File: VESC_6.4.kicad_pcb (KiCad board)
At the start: 4 copper layers, 62 x 60 mm, 389 parts, among them J1 CAN, J10 SUPPLY, J11 GND, J2 HALL_ENC, J3 COMM, J4 SERVO, J5 SWD, J6 USB_OTG, J7 PH_A, J8 PH_B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

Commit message: sometimes the gremlins would delete all of the save buttons work!
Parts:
- moved SW1 0.44 mm to (128.7, 67.2)
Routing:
- net /MCU/HALL_3: track 20.6 -> 58.7 mm, vias 0 -> 2
- net /MCU/HALL_2: track 16.5 -> 52.4 mm, vias 0 -> 2
- net /DRV/SDO: track 0.00 -> 30.3 mm, vias 0 -> 2
- net /DRV/SDI: track 0.00 -> 29.1 mm, vias 0 -> 2
- net /DRV/SCLK: track 0.00 -> 28.1 mm, vias 0 -> 2
- net /DRV/FAULT: track 0.00 -> 28.0 mm, vias 0 -> 2
- net /DRV/EN_GATE: track 0.00 -> 24.6 mm, vias 0 -> 3
- net /MCU/HALL_1: track 12.8 -> 33.6 mm, vias 0 -> 1
- net /MCU/ADC_TEMP: track 8.85 -> 25.4 mm, vias 0 -> 4
- net /DRV/CS: track 0.00 -> 3.13 mm, vias 0 -> 1
- net /MCU/H2: track 0.00 -> 3.07 mm, vias 0 -> 1
- net /MCU/H1: track 0.00 -> 2.75 mm, vias 0 -> 1
- net /MCU/H3: track 0.00 -> 2.60 mm, vias 0 -> 1
- net /MCU/TEMP_MOTOR: track 65.6 -> 66.4 mm
- net /DRV/INL_C: track 24.8 -> 24.3 mm

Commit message: dun dun dun
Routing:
- net /MCU/HALL_1: track 33.6 -> 69.4 mm, vias 1 -> 2
- net /DRV/CS: track 3.13 -> 32.2 mm, vias 1 -> 2
- net /MCU/H1: track 2.75 -> 27.2 mm, vias 1 -> 2
- net /MCU/HALL_2: track 52.4 -> 74.7 mm
- net /MCU/HALL_3: track 58.7 -> 80.2 mm
- net /DRV/EN_GATE: track 24.6 -> 25.8 mm
- net /DRV/FAULT: track 28.0 -> 28.7 mm
- net /DRV/SCLK: track 28.1 -> 28.8 mm
- net /DRV/SDI: track 29.1 -> 29.7 mm
- net /DRV/SDO: track 30.3 -> 30.9 mm

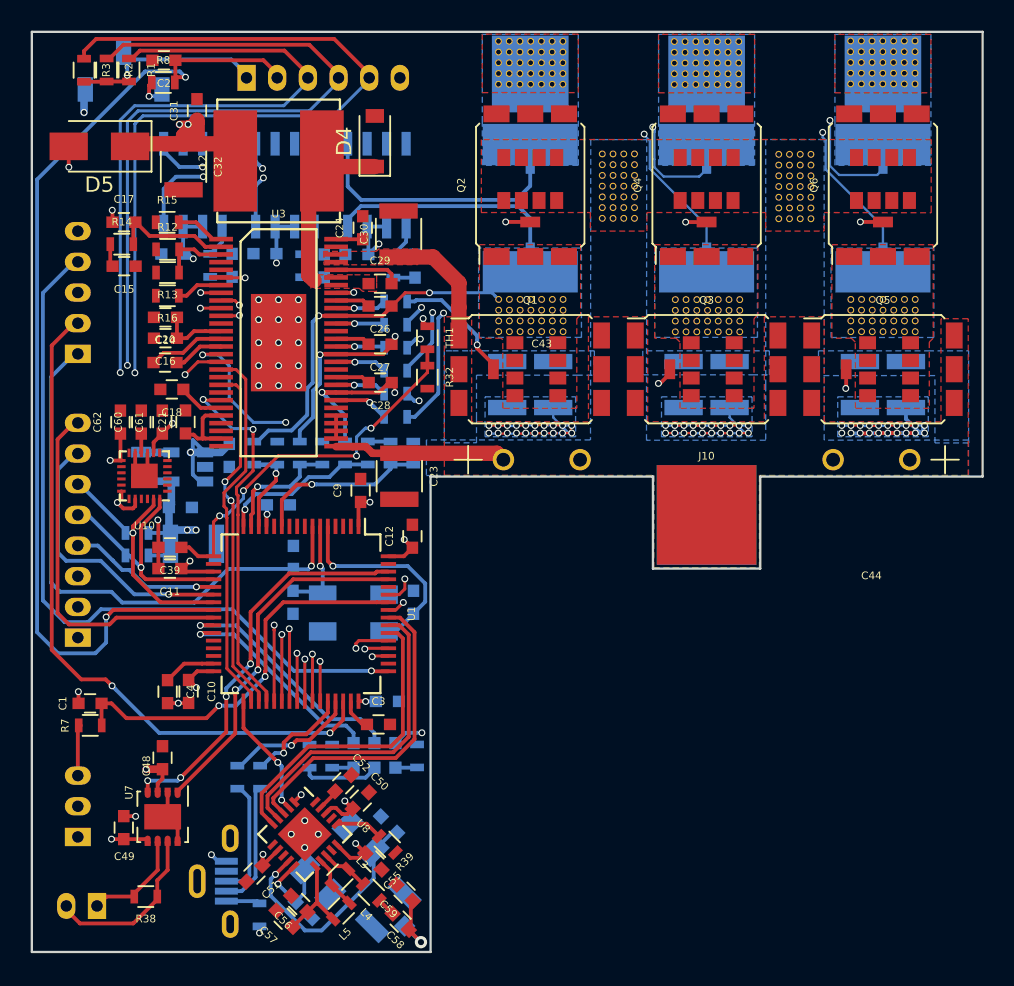
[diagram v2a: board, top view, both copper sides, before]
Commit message: something ate the power electronics ground plane!
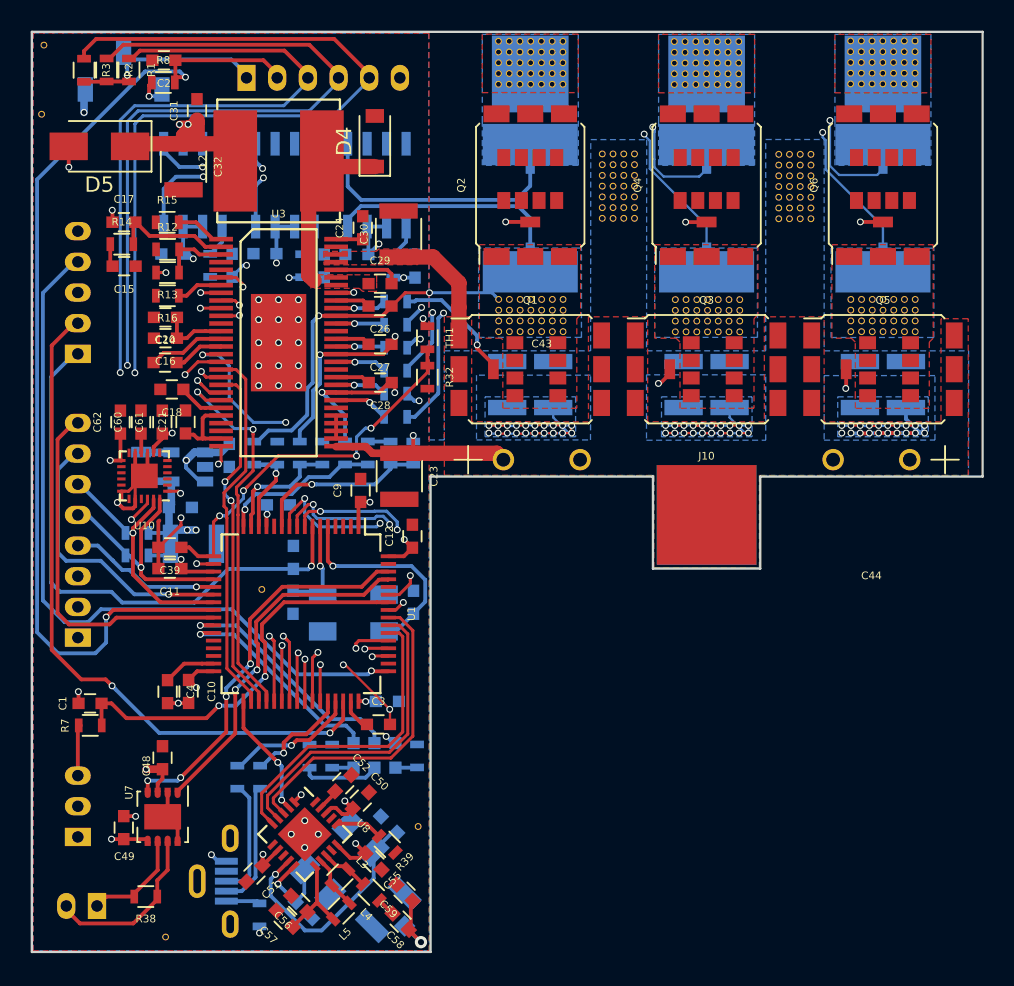
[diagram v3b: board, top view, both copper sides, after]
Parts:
- added ?: , Global_Parts:via-0.45mm, F.Cu at (137.7, 101.0)
- added ?: , Global_Parts:via-0.45mm, F.Cu at (131.4, 123.6)
- added ?: , Global_Parts:via-0.45mm, F.Cu at (147.9, 116.4)
- added ?: , Global_Parts:via-0.45mm, F.Cu at (123.3, 70.0)
- added ?: , Global_Parts:via-0.45mm, F.Cu at (123.5, 65.5)
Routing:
- net /MCU/CURRENT_3: track 1.43 -> 33.8 mm, vias 0 -> 3
- net /MCU/CURRENT_2: track 1.45 -> 30.9 mm, vias 0 -> 3
- net /MCU/CURRENT_1: track 1.42 -> 30.3 mm, vias 0 -> 3
- net /MCU/H3: track 2.60 -> 26.4 mm, vias 1 -> 2
- net /MCU/H2: track 3.07 -> 26.7 mm, vias 1 -> 2
- net GND: track 36.8 -> 49.4 mm, vias 27 -> 31
- net +5V: track 125.7 -> 134.2 mm, vias 6 -> 7
- net SUPPLY: track 59.1 -> 61.4 mm, vias 60 -> 61
- net /DRV/INL_C: track 24.2 -> 25.4 mm
- net VCC: track 59.5 -> 60.5 mm, vias 22 -> 24
- net /MCU/HALL_3: track 80.2 -> 79.2 mm
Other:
- net class Default: clearance 0.13 -> 0
- rule trace_clearance: 0.13 -> 0

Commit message: Rev1a done
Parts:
- added ?: MountingHole_3.2mm_M3, Mounting_Holes:MountingHole_3.2mm_M3, F.Cu at (161.0, 67.1)
- added ?: , Global_Parts:via-0.45mm, F.Cu at (144.9, 93.6)
- added ?: , Global_Parts:via-0.45mm, F.Cu at (147.6, 93.9)
- added ?: , Global_Parts:via-0.45mm, F.Cu at (138.6, 75.3)
- added ?: , Global_Parts:via-0.45mm, F.Cu at (144.5, 74.6)
- added ?: , Global_Parts:via-0.45mm, F.Cu at (146.7, 74.5)
- added ?: , Global_Parts:via-0.45mm, F.Cu at (128.2, 112.4)
- added ?: , Global_Parts:via-0.45mm, F.Cu at (139.2, 123.9)
- added ?: , Global_Parts:via-0.45mm, F.Cu at (143.3, 123.9)
- added ?: , Global_Parts:via-0.45mm, F.Cu at (147.8, 119.4)
- added ?: , Global_Parts:via-0.45mm, F.Cu at (146.3, 113.7)
- added ?: MountingHole_3.2mm_M3, Mounting_Holes:MountingHole_3.2mm_M3, F.Cu at (172.5, 67.1)
- added ?: , Global_Parts:via-0.45mm, F.Cu at (148.0, 106.8)
- added ?: , Global_Parts:via-0.45mm, F.Cu at (137.2, 81.1)
- added ?: , Global_Parts:via-0.45mm, F.Cu at (138.3, 80.3)
- added ?: , Global_Parts:via-0.45mm, F.Cu at (139.9, 89.1)
- added ?: , Global_Parts:via-0.45mm, F.Cu at (130.6, 85.3)
- added ?: , Global_Parts:via-0.45mm, F.Cu at (130.0, 81.8)
- added ?: , Global_Parts:via-0.45mm, F.Cu at (131.3, 104.0)
- added ?: , Global_Parts:via-0.45mm, F.Cu at (129.1, 106.1)
- added ?: , Global_Parts:via-0.45mm, F.Cu at (129.3, 110.5)
- added ?: , Global_Parts:via-0.45mm, F.Cu at (136.5, 111.1)
- added ?: , Global_Parts:via-0.45mm, F.Cu at (134.4, 114.1)
- added ?: , Global_Parts:via-0.45mm, F.Cu at (137.3, 98.2)
- added ?: , Global_Parts:via-0.45mm, F.Cu at (144.4, 98.5)
- added ?: , Global_Parts:via-0.45mm, F.Cu at (146.4, 83.6)
- added ?: , Global_Parts:via-0.45mm, F.Cu at (146.4, 86.3)
- added ?: , Global_Parts:via-0.45mm, F.Cu at (129.4, 68.6)
- moved R38 1.01 mm to (130.2, 122.0), turned to 90 degrees
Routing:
- net GND: track 49.4 -> 64.0 mm, vias 31 -> 35
- net /DRV/SH_A: track 23.5 -> 31.8 mm
- net /DRV/SH_B: track 30.5 -> 34.5 mm
- net +5V: track 134.2 -> 130.5 mm
- net /DRV/SH_C: track 40.7 -> 42.5 mm
- net /CAN/CANL: track 6.77 -> 7.55 mm
- net /CAN/CANH: track 11.4 -> 12.0 mm
- added copper zone on F.Cu, net +5V

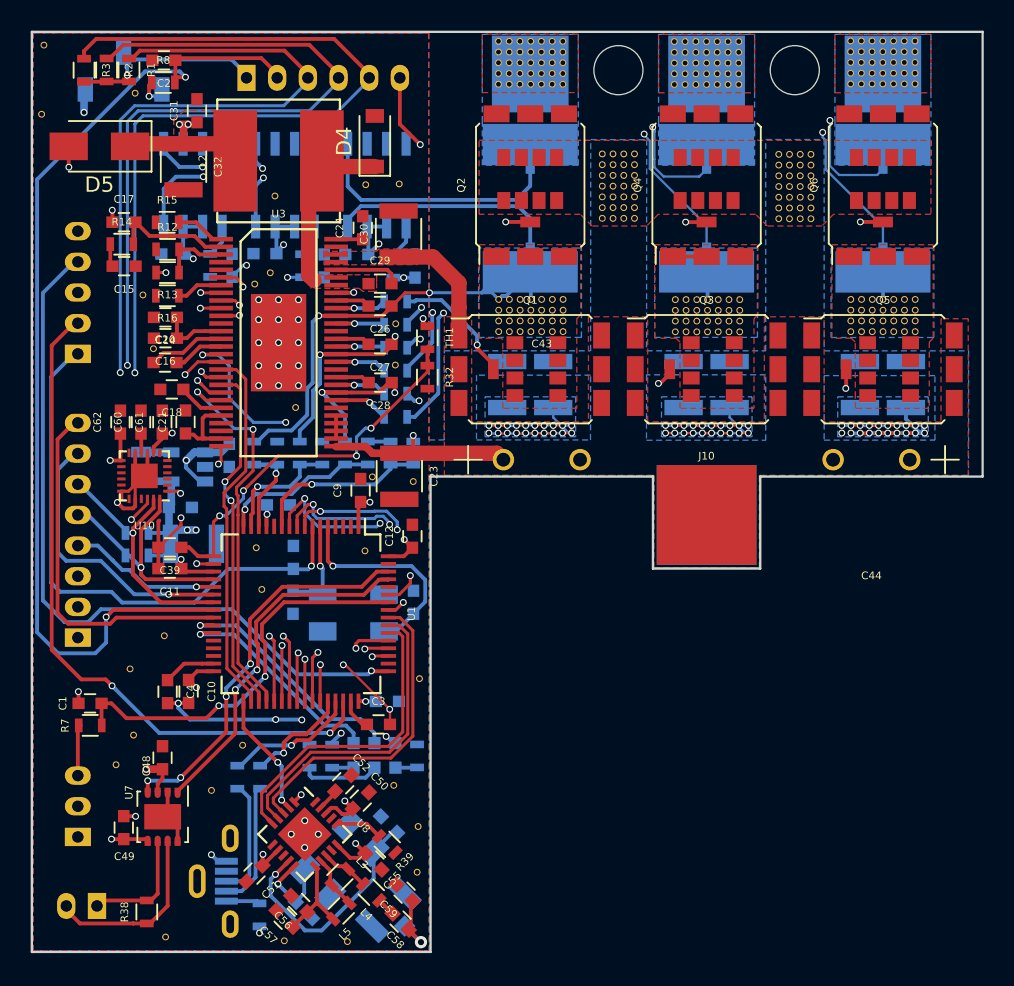
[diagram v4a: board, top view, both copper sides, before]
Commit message: changed the USB port around added CAD stuff
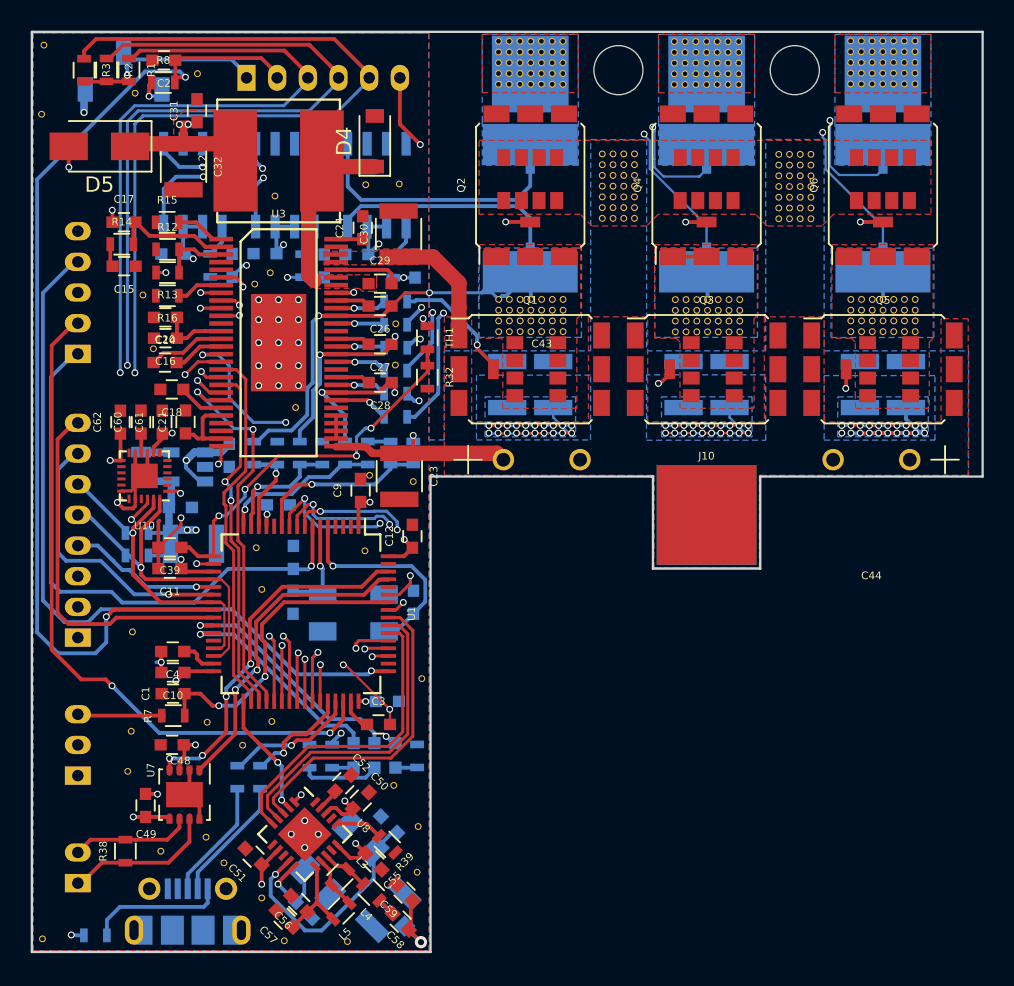
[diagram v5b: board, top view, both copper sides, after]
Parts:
- removed the ? at (131.3, 104.0)
- removed the ? at (131.4, 123.6)
- added ?: , Global_Parts:via-0.45mm, F.Cu at (133.5, 67.3)
- added ?: , Global_Parts:via-0.45mm, F.Cu at (123.4, 123.7)
- added ?: , Global_Parts:via-0.45mm, F.Cu at (135.2, 118.8)
- added ?: , Global_Parts:via-0.45mm, F.Cu at (137.7, 121.1)
- added ?: , Global_Parts:via-0.45mm, F.Cu at (134.1, 117.1)
- added ?: , Global_Parts:via-0.45mm, F.Cu at (131.1, 118.0)
- added ?: , Global_Parts:via-0.45mm, F.Cu at (134.1, 109.6)
- added G***: LOGO, Global_Parts:Kaly_LOGO, B.Cu at (131.2, 107.0)
- J6: footprint Connectors_USB:USB_Micro-B_Vertical_Molex-105133-0001 -> Connector_USB:USB_Micro-B_Molex-105017-0001
- moved R4 10.8 mm to (126.9, 123.5), turned to 0 degrees
- moved ? 9.06 mm to (138.4, 109.6)
- moved ? 5.60 mm to (129.0, 112.8)
- moved R7 5.45 mm to (131.9, 109.2)
- moved C1 5.45 mm to (131.9, 107.8)
- moved R38 4.20 mm to (128.8, 118.0)
- moved J4 4.00 mm to (125.7, 113.1)
- moved C4 2.64 mm to (131.9, 105.0), turned to 180 degrees
- moved J6 2.59 mm to (132.9, 121.9), turned to 180 degrees
- moved ? 2.42 mm to (129.3, 103.7)
- moved ? 2.40 mm to (129.2, 110.2)
- moved C49 2.03 mm to (130.1, 115.0)
- moved U7 2.03 mm to (132.7, 114.3)
- moved J1 1.94 mm to (125.7, 120.1), turned to 90 degrees
- moved C10 1.61 mm to (131.9, 106.4), turned to 180 degrees
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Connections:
- J1 pad 1: /CAN/CANL -> /CAN/CANH
- J1 pad 2: /CAN/CANH -> /CAN/CANL
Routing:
- net +5V: track 130.5 -> 119.1 mm
- net GND: track 64.0 -> 53.3 mm, vias 35 -> 31
- net Net-(J6-Pad1): track 2.22 -> 8.96 mm
- net /MCU/RX_SDA_NSS: track 16.0 -> 22.4 mm
- net /MCU/SERVO: track 26.0 -> 20.1 mm
- net /MPU9250/SCL: track 16.5 -> 20.7 mm
- net Net-(J4-Pad3): track 3.36 -> 5.79 mm
- net /MCU/CAN_TX: track 25.6 -> 23.6 mm
- net /MCU/CAN_RX: track 23.2 -> 21.3 mm
- net /CAN/CANH: track 12.0 -> 10.4 mm
- net Net-(C4-Pad1): track 3.45 -> 2.40 mm
- net VCC: track 61.0 -> 61.6 mm
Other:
- board text added: "Rev1a 3/4/2018"
